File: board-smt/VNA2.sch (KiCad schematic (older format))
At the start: 61 parts, among them U2 LM339, U3 SA612, U4 SA612, U5 SA612, U6 LM358, U7 LM358

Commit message: Adds SD card support, which is mandatory.  Also changed firmware for new pinouts.
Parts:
- L3, L4, L5: LCSC C1017 -> C1015
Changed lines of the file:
@@
 F 2 "Inductors_SMD:L_0805_HandSoldering" V 2830 1000 50  0001 C CNN
 F 3 "" H 2900 1000 50  0001 C CNN
-F 4 "C1017" H 2900 1000 60  0001 C CNN "LCSC"
+F 4 "C1015" H 2900 1000 60  0001 C CNN "LCSC"
 	1    2900 1000
 	-1   0    0    1
@@
 F 2 "Inductors_SMD:L_0805_HandSoldering" V 2780 2800 50  0001 C CNN
 F 3 "" H 2850 2800 50  0001 C CNN
-F 4 "C1017" H 2850 2800 60  0001 C CNN "LCSC"
+F 4 "C1015" H 2850 2800 60  0001 C CNN "LCSC"
 	1    2850 2800
 	-1   0    0    1
@@
 F 2 "Inductors_SMD:L_0805_HandSoldering" V 2980 4850 50  0001 C CNN
 F 3 "" H 3050 4850 50  0001 C CNN
-F 4 "C1017" H 3050 4850 60  0001 C CNN "LCSC"
+F 4 "C1015" H 3050 4850 60  0001 C CNN "LCSC"
 	1    3050 4850
 	-1   0    0    1

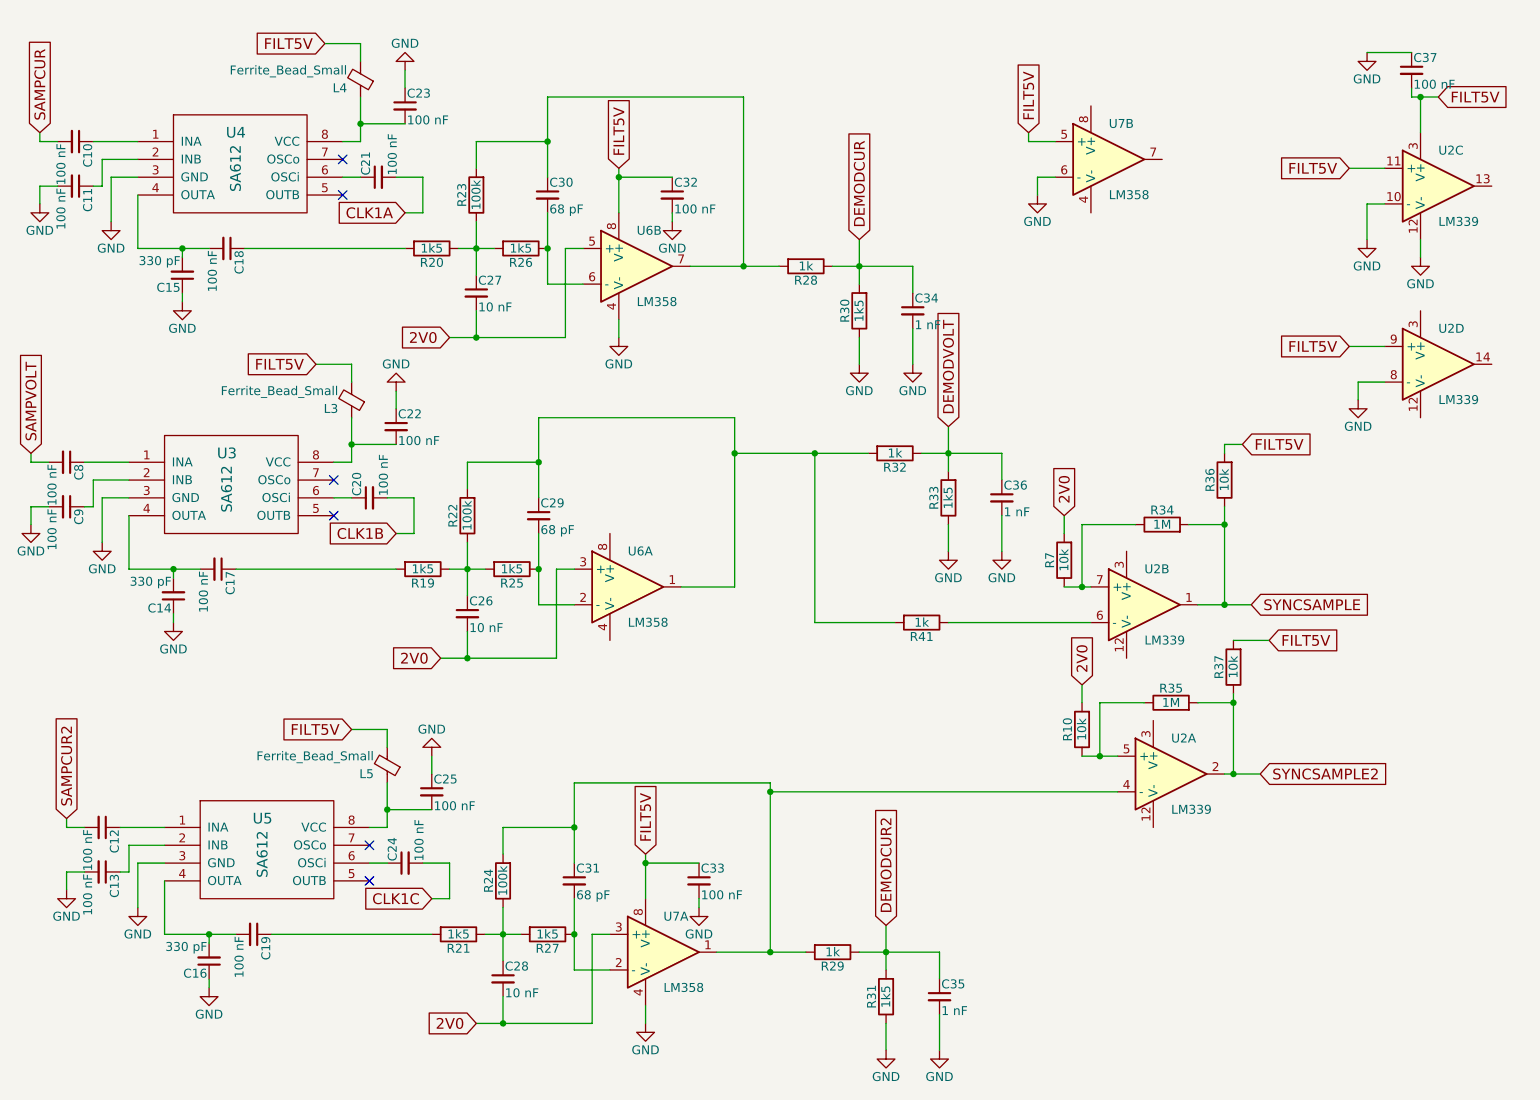
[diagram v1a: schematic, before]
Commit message: Finally removed the bluepill!
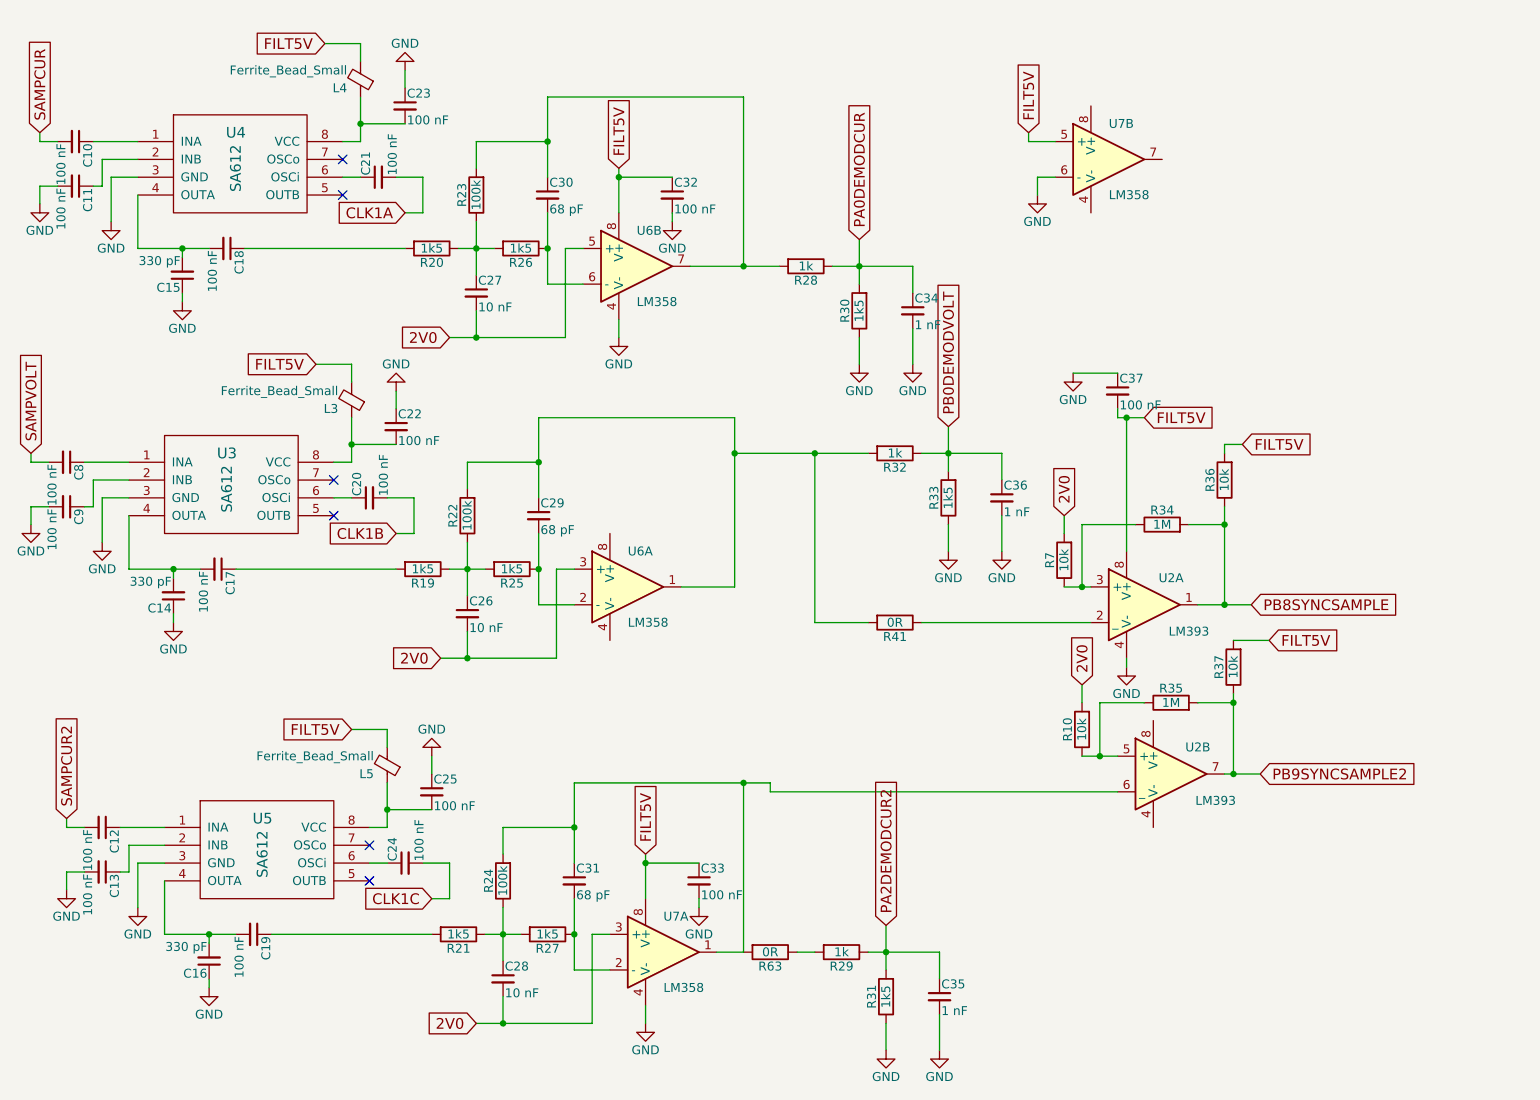
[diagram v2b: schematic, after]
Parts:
- removed U2: LM339, Housings_SOIC:SOIC-14_3.9x8.7mm_Pitch1.27mm, symbol LM339
- added R63: 0R, Resistors_SMD:R_0805_HandSoldering, symbol R
- added U2: LM393, Housings_SOIC:SOIC-8_3.9x4.9mm_Pitch1.27mm, symbol LM393
- R41: value 1k -> 0R; LCSC C17513 -> C17477
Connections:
- net FILT5V: now also U2.8 (V+)
- net GND: now also U2.4 (V-)
- net at C31.1, R24.2, U7.1: now also R63.2, U2.6 (_); no longer R29.2
- net at R10.1, R35.1: now also U2.5 (+)
- net at R34.1, R7.1: now also U2.3 (+)
- net at R41.1: now also U2.2 (_)
- net DEMODCUR renamed PA0DEMODCUR
- net DEMODCUR2 renamed PA2DEMODCUR2
- net DEMODVOLT renamed PB0DEMODVOLT
- net SYNCSAMPLE renamed PB8SYNCSAMPLE
- net PB8SYNCSAMPLE: now also U2.1
- net SYNCSAMPLE2 renamed PB9SYNCSAMPLE2
- net PB9SYNCSAMPLE2: now also U2.7
- new net: R29.2, R63.1
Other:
- moved on the sheet: C37, R29, R41

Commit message: Choke bridge
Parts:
- R30, R31, R33: value 1k5 -> 2k2; LCSC C4310 -> C17520
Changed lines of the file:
@@
 $EndComp
 $Comp
-L GND #PWR086
+L GND #PWR089
 U 1 1 5BB32DBE
 P 3150 950
-F 0 "#PWR086" H 3150 700 50  0001 C CNN
+F 0 "#PWR089" H 3150 700 50  0001 C CNN
 F 1 "GND" H 3150 800 50  0000 C CNN
 F 2 "" H 3150 950 50  0001 C CNN
@@
 $EndComp
 $Comp
-L GND #PWR087
+L GND #PWR090
 U 1 1 5BB32DD3
 P 1100 1700
-F 0 "#PWR087" H 1100 1450 50  0001 C CNN
+F 0 "#PWR090" H 1100 1450 50  0001 C CNN
 F 1 "GND" H 1100 1550 50  0000 C CNN
 F 2 "" H 1100 1700 50  0001 C CNN
@@
 $EndComp
 $Comp
-L GND #PWR088
+L GND #PWR091
 U 1 1 5BB32DD9
 P 1500 1800
-F 0 "#PWR088" H 1500 1550 50  0001 C CNN
+F 0 "#PWR091" H 1500 1550 50  0001 C CNN
 F 1 "GND" H 1500 1650 50  0000 C CNN
 F 2 "" H 1500 1800 50  0001 C CNN
@@
 $EndComp
 $Comp
-L GND #PWR089
+L GND #PWR092
 U 1 1 5BB32DF0
 P 1900 2250
-F 0 "#PWR089" H 1900 2000 50  0001 C CNN
+F 0 "#PWR092" H 1900 2000 50  0001 C CNN
 F 1 "GND" H 1900 2100 50  0000 C CNN
 F 2 "" H 1900 2250 50  0001 C CNN
@@
 $EndComp
 $Comp
-L GND #PWR090
+L GND #PWR093
 U 1 1 5BB32E0B
 P 4350 2450
-F 0 "#PWR090" H 4350 2200 50  0001 C CNN
+F 0 "#PWR093" H 4350 2200 50  0001 C CNN
 F 1 "GND" H 4350 2300 50  0000 C CNN
 F 2 "" H 4350 2450 50  0001 C CNN
@@
 FILT5V
 $Comp
-L GND #PWR091
+L GND #PWR094
 U 1 1 5BB32E19
 P 4650 1800
-F 0 "#PWR091" H 4650 1550 50  0001 C CNN
+F 0 "#PWR094" H 4650 1550 50  0001 C CNN
 F 1 "GND" H 4650 1650 50  0000 C CNN
 F 2 "" H 4650 1800 50  0001 C CNN
@@
 $EndComp
 $Comp
-L GND #PWR092
+L GND #PWR095
 U 1 1 5BB32E52
 P 3100 2750
-F 0 "#PWR092" H 3100 2500 50  0001 C CNN
+F 0 "#PWR095" H 3100 2500 50  0001 C CNN
 F 1 "GND" H 3100 2600 50  0000 C CNN
 F 2 "" H 3100 2750 50  0001 C CNN
@@
 $EndComp
 $Comp
-L GND #PWR093
+L GND #PWR096
 U 1 1 5BB32E67
 P 1050 3500
-F 0 "#PWR093" H 1050 3250 50  0001 C CNN
+F 0 "#PWR096" H 1050 3250 50  0001 C CNN
 F 1 "GND" H 1050 3350 50  0000 C CNN
 F 2 "" H 1050 3500 50  0001 C CNN
@@
 $EndComp
 $Comp
-L GND #PWR094
+L GND #PWR097
 U 1 1 5BB32E6D
 P 1450 3600
-F 0 "#PWR094" H 1450 3350 50  0001 C CNN
+F 0 "#PWR097" H 1450 3350 50  0001 C CNN
 F 1 "GND" H 1450 3450 50  0000 C CNN
 F 2 "" H 1450 3600 50  0001 C CNN
@@
 $EndComp
 $Comp
-L GND #PWR095
+L GND #PWR098
 U 1 1 5BB32E84
 P 1850 4050
-F 0 "#PWR095" H 1850 3800 50  0001 C CNN
+F 0 "#PWR098" H 1850 3800 50  0001 C CNN
 F 1 "GND" H 1850 3900 50  0000 C CNN
 F 2 "" H 1850 4050 50  0001 C CNN
@@
 P 5700 2300
 F 0 "R30" V 5780 2300 50  0000 C CNN
-F 1 "1k5" V 5700 2300 50  0000 C CNN
+F 1 "2k2" V 5700 2300 50  0000 C CNN
 F 2 "Resistors_SMD:R_0805_HandSoldering" V 5630 2300 50  0001 C CNN
 F 3 "" H 5700 2300 50  0001 C CNN
-F 4 "C4310" V 5700 2300 60  0001 C CNN "LCSC"
+F 4 "C17520" V 5700 2300 60  0001 C CNN "LCSC"
 	1    5700 2300
 	-1   0    0    1
 $EndComp
 $Comp
-L GND #PWR096
+L GND #PWR099
 U 1 1 5BB32ED8
 P 5700 2600
-F 0 "#PWR096" H 5700 2350 50  0001 C CNN
+F 0 "#PWR099" H 5700 2350 50  0001 C CNN
 F 1 "GND" H 5700 2450 50  0000 C CNN
 F 2 "" H 5700 2600 50  0001 C CNN
@@
 $EndComp
 $Comp
-L GND #PWR097
+L GND #PWR0100
 U 1 1 5BB32EE5
 P 6000 2600
-F 0 "#PWR097" H 6000 2350 50  0001 C CNN
+F 0 "#PWR0100" H 6000 2350 50  0001 C CNN
 F 1 "GND" H 6000 2450 50  0000 C CNN
 F 2 "" H 6000 2600 50  0001 C CNN
@@
 P 6200 3350
 F 0 "R33" V 6280 3350 50  0000 C CNN
-F 1 "1k5" V 6200 3350 50  0000 C CNN
+F 1 "2k2" V 6200 3350 50  0000 C CNN
 F 2 "Resistors_SMD:R_0805_HandSoldering" V 6130 3350 50  0001 C CNN
 F 3 "" H 6200 3350 50  0001 C CNN
-F 4 "C4310" V 6200 3350 60  0001 C CNN "LCSC"
+F 4 "C17520" V 6200 3350 60  0001 C CNN "LCSC"
 	1    6200 3350
 	-1   0    0    1
 $EndComp
 $Comp
-L GND #PWR098
+L GND #PWR0101
 U 1 1 5BB32EFA
 P 6200 3650
-F 0 "#PWR098" H 6200 3400 50  0001 C CNN
+F 0 "#PWR0101" H 6200 3400 50  0001 C CNN
 F 1 "GND" H 6200 3500 50  0000 C CNN
 F 2 "" H 6200 3650 50  0001 C CNN
@@
 $EndComp
 $Comp
-L GND #PWR099
+L GND #PWR0102
 U 1 1 5BB32F07
 P 6500 3650
-F 0 "#PWR099" H 6500 3400 50  0001 C CNN
+F 0 "#PWR0102" H 6500 3400 50  0001 C CNN
 F 1 "GND" H 6500 3500 50  0000 C CNN
 F 2 "" H 6500 3650 50  0001 C CNN
@@
 $EndComp
 $Comp
-L GND #PWR0100
+L GND #PWR0103
 U 1 1 5BB496C5
 P 3300 4800
-F 0 "#PWR0100" H 3300 4550 50  0001 C CNN
+F 0 "#PWR0103" H 3300 4550 50  0001 C CNN
 F 1 "GND" H 3300 4650 50  0000 C CNN
 F 2 "" H 3300 4800 50  0001 C CNN
@@
 $EndComp
 $Comp
-L GND #PWR0101
+L GND #PWR0104
 U 1 1 5BB496D8
 P 1250 5550
-F 0 "#PWR0101" H 1250 5300 50  0001 C CNN
+F 0 "#PWR0104" H 1250 5300 50  0001 C CNN
 F 1 "GND" H 1250 5400 50  0000 C CNN
 F 2 "" H 1250 5550 50  0001 C CNN
@@
 $EndComp
 $Comp
-L GND #PWR0102
+L GND #PWR0105
 U 1 1 5BB496DE
 P 1650 5650
-F 0 "#PWR0102" H 1650 5400 50  0001 C CNN
+F 0 "#PWR0105" H 1650 5400 50  0001 C CNN
 F 1 "GND" H 1650 5500 50  0000 C CNN
 F 2 "" H 1650 5650 50  0001 C CNN
@@
 $EndComp
 $Comp
-L GND #PWR0103
+L GND #PWR0106
 U 1 1 5BB496F3
 P 2050 6100
-F 0 "#PWR0103" H 2050 5850 50  0001 C CNN
+F 0 "#PWR0106" H 2050 5850 50  0001 C CNN
 F 1 "GND" H 2050 5950 50  0000 C CNN
 F 2 "" H 2050 6100 50  0001 C CNN
@@
 $EndComp
 $Comp
-L GND #PWR0104
+L GND #PWR0107
 U 1 1 5BB4970B
 P 4500 6300
-F 0 "#PWR0104" H 4500 6050 50  0001 C CNN
+F 0 "#PWR0107" H 4500 6050 50  0001 C CNN
 F 1 "GND" H 4500 6150 50  0000 C CNN
 F 2 "" H 4500 6300 50  0001 C CNN
@@
 FILT5V
 $Comp
-L GND #PWR0105
+L GND #PWR0108
 U 1 1 5BB49718
 P 4800 5650
-F 0 "#PWR0105" H 4800 5400 50  0001 C CNN
+F 0 "#PWR0108" H 4800 5400 50  0001 C CNN
 F 1 "GND" H 4800 5500 50  0000 C CNN
 F 2 "" H 4800 5650 50  0001 C CNN
@@
 P 5850 6150
 F 0 "R31" V 5930 6150 50  0000 C CNN
-F 1 "1k5" V 5850 6150 50  0000 C CNN
+F 1 "2k2" V 5850 6150 50  0000 C CNN
 F 2 "Resistors_SMD:R_0805_HandSoldering" V 5780 6150 50  0001 C CNN
 F 3 "" H 5850 6150 50  0001 C CNN
-F 4 "C4310" V 5850 6150 60  0001 C CNN "LCSC"
+F 4 "C17520" V 5850 6150 60  0001 C CNN "LCSC"
 	1    5850 6150
 	-1   0    0    1
 $EndComp
 $Comp
-L GND #PWR0106
+L GND #PWR0109
 U 1 1 5BB4974C
 P 5850 6450
-F 0 "#PWR0106" H 5850 6200 50  0001 C CNN
+F 0 "#PWR0109" H 5850 6200 50  0001 C CNN
 F 1 "GND" H 5850 6300 50  0000 C CNN
 F 2 "" H 5850 6450 50  0001 C CNN
@@
 $EndComp
 $Comp
-L GND #PWR0107
+L GND #PWR0110
 U 1 1 5BB49758
 P 6150 6450
-F 0 "#PWR0107" H 6150 6200 50  0001 C CNN
+F 0 "#PWR0110" H 6150 6200 50  0001 C CNN
 F 1 "GND" H 6150 6300 50  0000 C CNN
 F 2 "" H 6150 6450 50  0001 C CNN
@@
 $EndComp
 $Comp
-L GND #PWR0108
+L GND #PWR0111
 U 1 1 5BB4F877
 P 6700 1650
-F 0 "#PWR0108" H 6700 1400 50  0001 C CNN
+F 0 "#PWR0111" H 6700 1400 50  0001 C CNN
 F 1 "GND" H 6700 1500 50  0000 C CNN
 F 2 "" H 6700 1650 50  0001 C CNN
@@
 $EndComp
 $Comp
-L GND #PWR0109
+L GND #PWR0112
 U 1 1 5BF2333C
 P 6900 2650
-F 0 "#PWR0109" H 6900 2400 50  0001 C CNN
+F 0 "#PWR0112" H 6900 2400 50  0001 C CNN
 F 1 "GND" H 6900 2500 50  0000 C CNN
 F 2 "" H 6900 2650 50  0001 C CNN
@@
 $EndComp
 $Comp
-L GND #PWR0110
+L GND #PWR0113
 U 1 1 5ECEC848
 P 7200 4300
-F 0 "#PWR0110" H 7200 4050 50  0001 C CNN
+F 0 "#PWR0113" H 7200 4050 50  0001 C CNN
 F 1 "GND" H 7200 4150 50  0000 C CNN
 F 2 "" H 7200 4300 50  0001 C CNN

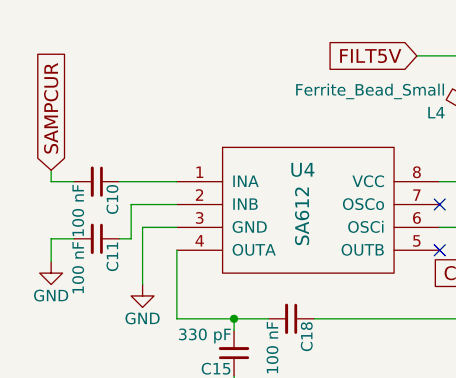
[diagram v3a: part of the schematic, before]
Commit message: Changed to resistive bridge
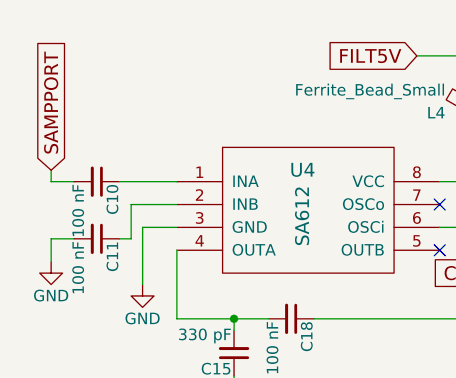
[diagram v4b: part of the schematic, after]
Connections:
- net SAMPCUR renamed SAMPPORT
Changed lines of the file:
@@
 $EndComp
 $Comp
-L GND #PWR089
+L GND #PWR98
 U 1 1 5BB32DBE
 P 3150 950
-F 0 "#PWR089" H 3150 700 50  0001 C CNN
+F 0 "#PWR98" H 3150 700 50  0001 C CNN
 F 1 "GND" H 3150 800 50  0000 C CNN
 F 2 "" H 3150 950 50  0001 C CNN
@@
 $EndComp
 Text GLabel 1100 1300 1    60   Input ~ 0
-SAMPCUR
+SAMPPORT
 $Comp
 L C_Small C10
@@
 $EndComp
 $Comp
-L GND #PWR090
+L GND #PWR89
 U 1 1 5BB32DD3
 P 1100 1700
-F 0 "#PWR090" H 1100 1450 50  0001 C CNN
+F 0 "#PWR89" H 1100 1450 50  0001 C CNN
 F 1 "GND" H 1100 1550 50  0000 C CNN
 F 2 "" H 1100 1700 50  0001 C CNN
@@
 $EndComp
 $Comp
-L GND #PWR091
+L GND #PWR92
 U 1 1 5BB32DD9
 P 1500 1800
-F 0 "#PWR091" H 1500 1550 50  0001 C CNN
+F 0 "#PWR92" H 1500 1550 50  0001 C CNN
 F 1 "GND" H 1500 1650 50  0000 C CNN
 F 2 "" H 1500 1800 50  0001 C CNN
@@
 $EndComp
 $Comp
-L GND #PWR092
+L GND #PWR95
 U 1 1 5BB32DF0
 P 1900 2250
-F 0 "#PWR092" H 1900 2000 50  0001 C CNN
+F 0 "#PWR95" H 1900 2000 50  0001 C CNN
 F 1 "GND" H 1900 2100 50  0000 C CNN
 F 2 "" H 1900 2250 50  0001 C CNN
@@
 $EndComp
 $Comp
-L GND #PWR093
+L GND #PWR100
 U 1 1 5BB32E0B
 P 4350 2450
-F 0 "#PWR093" H 4350 2200 50  0001 C CNN
+F 0 "#PWR100" H 4350 2200 50  0001 C CNN
 F 1 "GND" H 4350 2300 50  0000 C CNN
 F 2 "" H 4350 2450 50  0001 C CNN
@@
 FILT5V
 $Comp
-L GND #PWR094
+L GND #PWR102
 U 1 1 5BB32E19
 P 4650 1800
-F 0 "#PWR094" H 4650 1550 50  0001 C CNN
+F 0 "#PWR102" H 4650 1550 50  0001 C CNN
 F 1 "GND" H 4650 1650 50  0000 C CNN
 F 2 "" H 4650 1800 50  0001 C CNN
@@
 $EndComp
 $Comp
-L GND #PWR095
+L GND #PWR97
 U 1 1 5BB32E52
 P 3100 2750
-F 0 "#PWR095" H 3100 2500 50  0001 C CNN
+F 0 "#PWR97" H 3100 2500 50  0001 C CNN
 F 1 "GND" H 3100 2600 50  0000 C CNN
 F 2 "" H 3100 2750 50  0001 C CNN
@@
 $EndComp
 $Comp
-L GND #PWR096
+L GND #PWR88
 U 1 1 5BB32E67
 P 1050 3500
-F 0 "#PWR096" H 1050 3250 50  0001 C CNN
+F 0 "#PWR88" H 1050 3250 50  0001 C CNN
 F 1 "GND" H 1050 3350 50  0000 C CNN
 F 2 "" H 1050 3500 50  0001 C CNN
@@
 $EndComp
 $Comp
-L GND #PWR097
+L GND #PWR91
 U 1 1 5BB32E6D
 P 1450 3600
-F 0 "#PWR097" H 1450 3350 50  0001 C CNN
+F 0 "#PWR91" H 1450 3350 50  0001 C CNN
 F 1 "GND" H 1450 3450 50  0000 C CNN
 F 2 "" H 1450 3600 50  0001 C CNN
@@
 $EndComp
 $Comp
-L GND #PWR098
+L GND #PWR94
 U 1 1 5BB32E84
 P 1850 4050
-F 0 "#PWR098" H 1850 3800 50  0001 C CNN
+F 0 "#PWR94" H 1850 3800 50  0001 C CNN
 F 1 "GND" H 1850 3900 50  0000 C CNN
 F 2 "" H 1850 4050 50  0001 C CNN
@@
 $EndComp
 $Comp
-L GND #PWR099
+L GND #PWR104
 U 1 1 5BB32ED8
 P 5700 2600
-F 0 "#PWR099" H 5700 2350 50  0001 C CNN
+F 0 "#PWR104" H 5700 2350 50  0001 C CNN
 F 1 "GND" H 5700 2450 50  0000 C CNN
 F 2 "" H 5700 2600 50  0001 C CNN
@@
 $EndComp
 $Comp
-L GND #PWR0100
+L GND #PWR106
 U 1 1 5BB32EE5
 P 6000 2600
-F 0 "#PWR0100" H 6000 2350 50  0001 C CNN
+F 0 "#PWR106" H 6000 2350 50  0001 C CNN
 F 1 "GND" H 6000 2450 50  0000 C CNN
 F 2 "" H 6000 2600 50  0001 C CNN
@@
 $EndComp
 $Comp
-L GND #PWR0101
+L GND #PWR108
 U 1 1 5BB32EFA
 P 6200 3650
-F 0 "#PWR0101" H 6200 3400 50  0001 C CNN
+F 0 "#PWR108" H 6200 3400 50  0001 C CNN
 F 1 "GND" H 6200 3500 50  0000 C CNN
 F 2 "" H 6200 3650 50  0001 C CNN
@@
 $EndComp
 $Comp
-L GND #PWR0102
+L GND #PWR109
 U 1 1 5BB32F07
 P 6500 3650
-F 0 "#PWR0102" H 6500 3400 50  0001 C CNN
+F 0 "#PWR109" H 6500 3400 50  0001 C CNN
 F 1 "GND" H 6500 3500 50  0000 C CNN
 F 2 "" H 6500 3650 50  0001 C CNN
@@
 $EndComp
 $Comp
-L GND #PWR0103
+L GND #PWR99
 U 1 1 5BB496C5
 P 3300 4800
-F 0 "#PWR0103" H 3300 4550 50  0001 C CNN
+F 0 "#PWR99" H 3300 4550 50  0001 C CNN
 F 1 "GND" H 3300 4650 50  0000 C CNN
 F 2 "" H 3300 4800 50  0001 C CNN
@@
 $EndComp
 $Comp
-L GND #PWR0104
+L GND #PWR90
 U 1 1 5BB496D8
 P 1250 5550
-F 0 "#PWR0104" H 1250 5300 50  0001 C CNN
+F 0 "#PWR90" H 1250 5300 50  0001 C CNN
 F 1 "GND" H 1250 5400 50  0000 C CNN
 F 2 "" H 1250 5550 50  0001 C CNN
@@
 $EndComp
 $Comp
-L GND #PWR0105
+L GND #PWR93
 U 1 1 5BB496DE
 P 1650 5650
-F 0 "#PWR0105" H 1650 5400 50  0001 C CNN
+F 0 "#PWR93" H 1650 5400 50  0001 C CNN
 F 1 "GND" H 1650 5500 50  0000 C CNN
 F 2 "" H 1650 5650 50  0001 C CNN
@@
 $EndComp
 $Comp
-L GND #PWR0106
+L GND #PWR96
 U 1 1 5BB496F3
 P 2050 6100
-F 0 "#PWR0106" H 2050 5850 50  0001 C CNN
+F 0 "#PWR96" H 2050 5850 50  0001 C CNN
 F 1 "GND" H 2050 5950 50  0000 C CNN
 F 2 "" H 2050 6100 50  0001 C CNN
@@
 $EndComp
 $Comp
-L GND #PWR0107
+L GND #PWR101
 U 1 1 5BB4970B
 P 4500 6300
-F 0 "#PWR0107" H 4500 6050 50  0001 C CNN
+F 0 "#PWR101" H 4500 6050 50  0001 C CNN
 F 1 "GND" H 4500 6150 50  0000 C CNN
 F 2 "" H 4500 6300 50  0001 C CNN
@@
 FILT5V
 $Comp
-L GND #PWR0108
+L GND #PWR103
 U 1 1 5BB49718
 P 4800 5650
-F 0 "#PWR0108" H 4800 5400 50  0001 C CNN
+F 0 "#PWR103" H 4800 5400 50  0001 C CNN
 F 1 "GND" H 4800 5500 50  0000 C CNN
 F 2 "" H 4800 5650 50  0001 C CNN
@@
 $EndComp
 $Comp
-L GND #PWR0109
+L GND #PWR105
 U 1 1 5BB4974C
 P 5850 6450
-F 0 "#PWR0109" H 5850 6200 50  0001 C CNN
+F 0 "#PWR105" H 5850 6200 50  0001 C CNN
 F 1 "GND" H 5850 6300 50  0000 C CNN
 F 2 "" H 5850 6450 50  0001 C CNN
@@
 $EndComp
 $Comp
-L GND #PWR0110
+L GND #PWR107
 U 1 1 5BB49758
 P 6150 6450
-F 0 "#PWR0110" H 6150 6200 50  0001 C CNN
+F 0 "#PWR107" H 6150 6200 50  0001 C CNN
 F 1 "GND" H 6150 6300 50  0000 C CNN
 F 2 "" H 6150 6450 50  0001 C CNN
@@
 $EndComp
 $Comp
-L GND #PWR0111
+L GND #PWR110
 U 1 1 5BB4F877
 P 6700 1650
-F 0 "#PWR0111" H 6700 1400 50  0001 C CNN
+F 0 "#PWR110" H 6700 1400 50  0001 C CNN
 F 1 "GND" H 6700 1500 50  0000 C CNN
 F 2 "" H 6700 1650 50  0001 C CNN
@@
 $EndComp
 $Comp
-L GND #PWR0112
+L GND #PWR111
 U 1 1 5BF2333C
 P 6900 2650
-F 0 "#PWR0112" H 6900 2400 50  0001 C CNN
+F 0 "#PWR111" H 6900 2400 50  0001 C CNN
 F 1 "GND" H 6900 2500 50  0000 C CNN
 F 2 "" H 6900 2650 50  0001 C CNN
@@
 $EndComp
 $Comp
-L GND #PWR0113
+L GND #PWR112
 U 1 1 5ECEC848
 P 7200 4300
-F 0 "#PWR0113" H 7200 4050 50  0001 C CNN
+F 0 "#PWR112" H 7200 4050 50  0001 C CNN
 F 1 "GND" H 7200 4150 50  0000 C CNN
 F 2 "" H 7200 4300 50  0001 C CNN
